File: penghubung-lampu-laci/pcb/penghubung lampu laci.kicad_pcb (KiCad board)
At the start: 2 copper layers, 49.5 x 27.3 mm, 13 parts

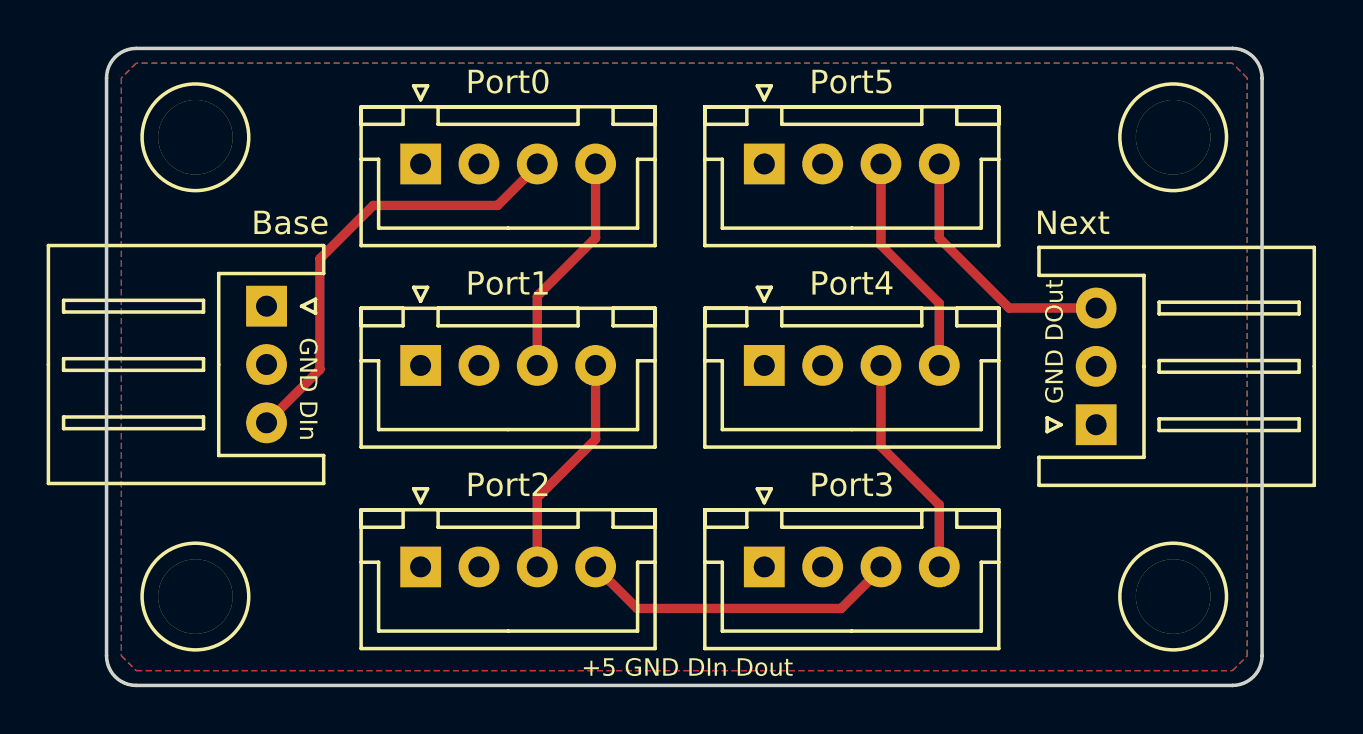
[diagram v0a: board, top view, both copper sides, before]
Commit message: Update pin order and component positions
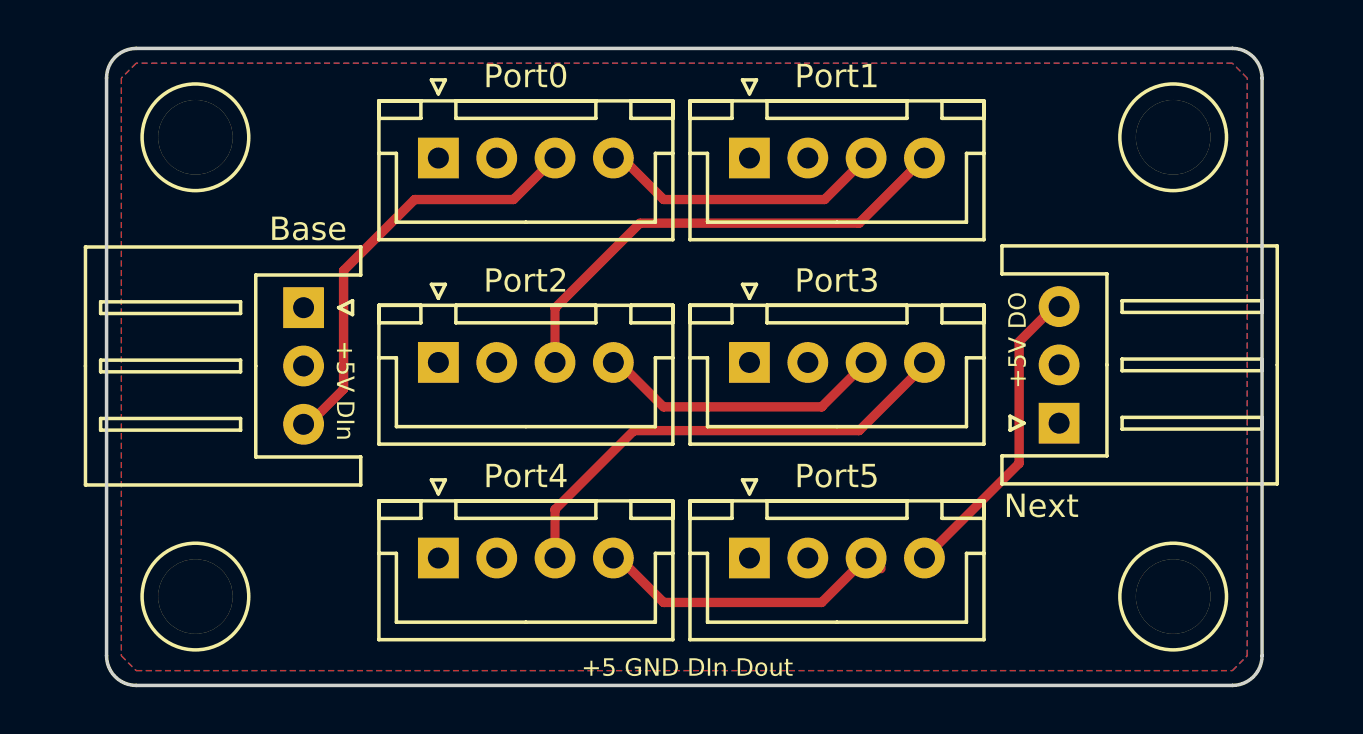
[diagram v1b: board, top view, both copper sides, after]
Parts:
- moved Port5 16.9 mm to (166.0, 129.2)
- moved Port1 16.7 mm to (166.0, 112.0)
- moved Port4 16.2 mm to (152.7, 129.2)
- moved Port2 8.80 mm to (152.7, 120.8)
- moved Port3 8.79 mm to (166.0, 120.8)
- moved Next 1.59 mm to (179.3, 123.4)
- moved Base 1.59 mm to (146.9, 118.4)
- moved Port0 0.80 mm to (152.7, 112.0)
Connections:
- Base pad 1: +5V -> GND
- Base pad 2: GND -> +5V
- Next pad 1: +5V -> GND
- Next pad 2: GND -> +5V
- Port0 pad 1: +5V -> GND
- Port0 pad 2: GND -> +5V
- Port1 pad 1: +5V -> GND
- Port1 pad 2: GND -> +5V
- Port2 pad 1: +5V -> GND
- Port2 pad 2: GND -> +5V
- Port3 pad 1: +5V -> GND
- Port3 pad 2: GND -> +5V
- Port4 pad 1: +5V -> GND
- Port4 pad 2: GND -> +5V
- Port5 pad 1: +5V -> GND
- Port5 pad 2: GND -> +5V
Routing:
- net /Signal2: track 9.67 -> 20.8 mm
- net /Signal4: track 9.67 -> 20.6 mm
- net /Signal5: track 9.67 -> 12.8 mm
- net /Signal1: track 9.67 -> 12.4 mm
- net /SignalX: track 11.1 -> 13.4 mm
- net /Signal3: track 13.9 -> 12.7 mm
- net /Signal0: track 19.0 -> 18.5 mm
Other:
- board text added: "+5V DIn"
- board text added: "+5V DO"
- board text removed: "GND DIn"
- board text removed: "GND DOut"
